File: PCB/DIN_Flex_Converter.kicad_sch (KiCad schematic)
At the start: 14 parts

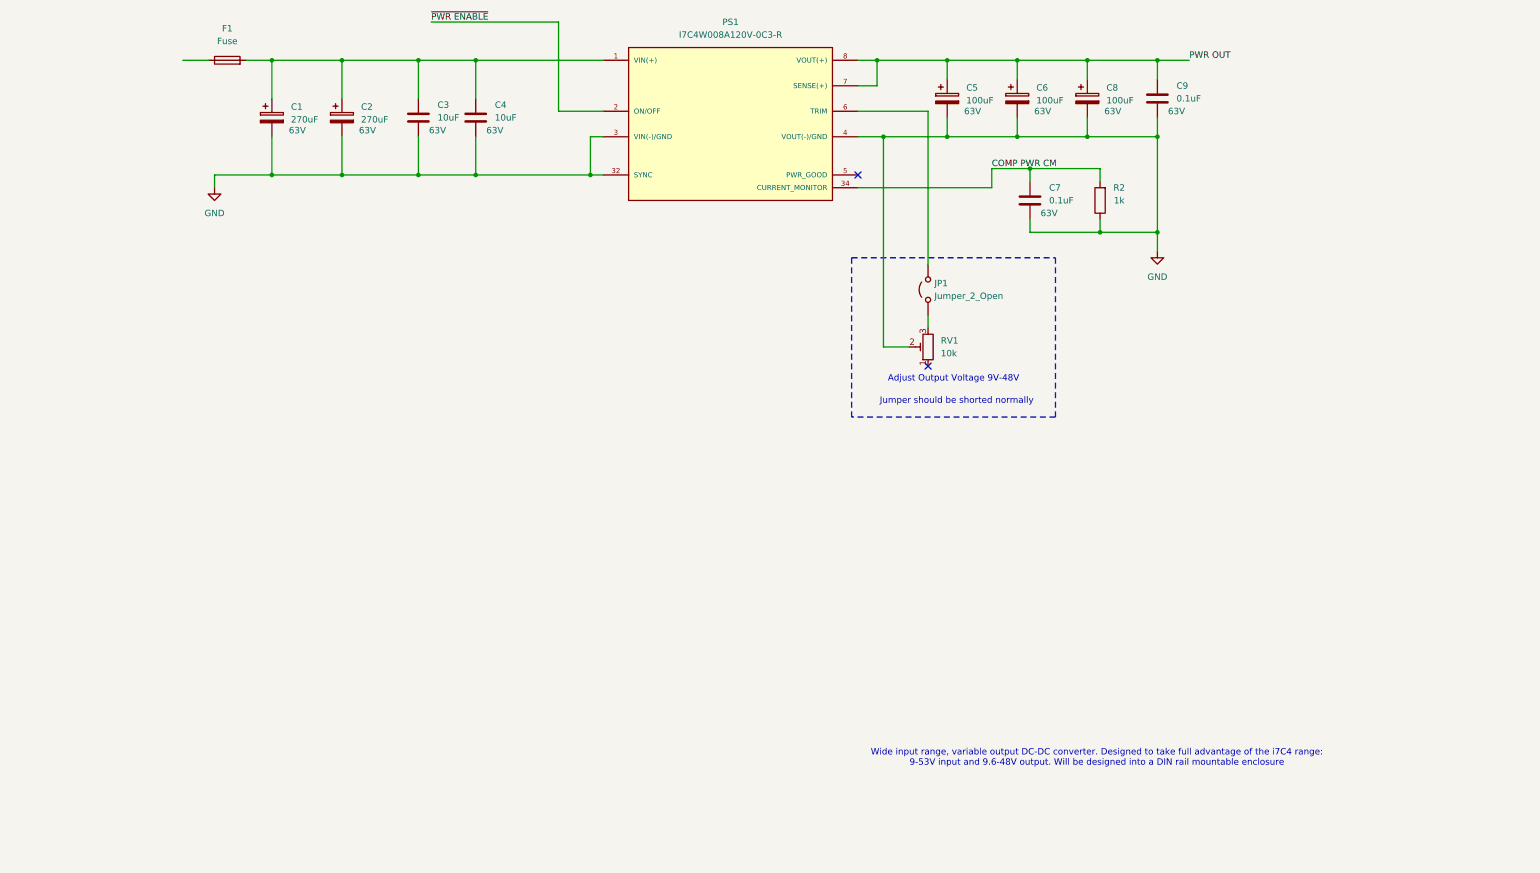
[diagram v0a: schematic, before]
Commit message: Added Trim & Linear Regulator
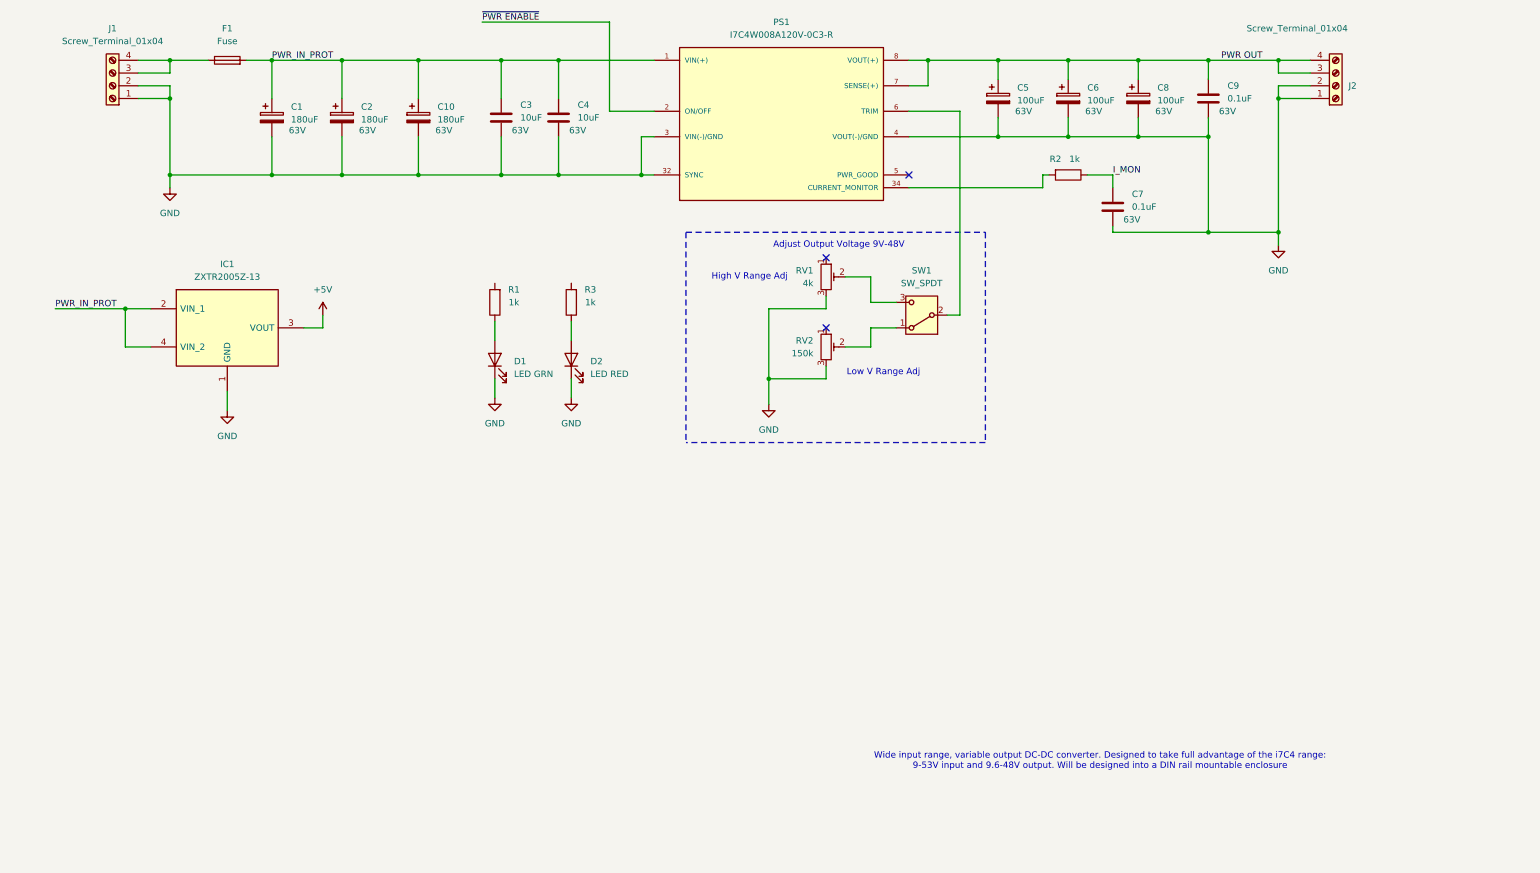
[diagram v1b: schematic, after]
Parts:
- removed JP1: Jumper_2_Open, Connector_PinHeader_2.54mm:PinHeader_1x02_P2.54mm_Vertical, symbol Jumper:Jumper_2_Open
- added C10: 180uF, Capacitor_SMD:CP_Elec_10x12.6, symbol Device:C_Polarized
- added D1: LED GRN, symbol Device:LED
- added D2: LED RED, symbol Device:LED
- added IC1: ZXTR2005Z-13, AZ7042RTRG1, symbol PSA:ZXTR2005Z-13
- added J1, J2: Screw_Terminal_01x04, symbol Connector:Screw_Terminal_01x04
- added R1, R3: 1k, Resistor_SMD:R_1206_3216Metric, symbol Device:R
- added RV2: 150k, PSA:Bourns PV37X, symbol Device:R_Potentiometer_Trim
- added SW1: SW_SPDT, symbol Switch:SW_SPDT
- C1, C2: value 270uF -> 180uF
- C9: footprint Capacitor_SMD:C_1210_3225Metric -> Capacitor_SMD:C_1206_3216Metric
- RV1: value 10k -> 4k
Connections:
- net GND: now also RV1.3, C10.2, D1.1 (K), D2.1 (K), IC1.1 (GND), J1.1 (Pin_1), J1.2 (Pin_2), J2.1 (Pin_1), J2.2 (Pin_2), RV2.3; no longer R2.1, RV1.2
- net PWR OUT: now also J2.3 (Pin_3), J2.4 (Pin_4)
- net PWR_IN_PROT: now reaches C1.1, C2.1, C3.1, C4.1, F1.2, PS1.1 (VIN(+))
- net PWR_IN_PROT: now also C10.1, IC1.2 (VIN_1), IC1.4 (VIN_2)
- net at PS1.6 (TRIM): now also SW1.2 (B)
- net at F1.1: now also J1.3 (Pin_3), J1.4 (Pin_4)
- net COMP PWR CM: no longer names the net of PS1.34 (CURRENT_MONITOR), R2.2
- net COMP PWR CM: no longer C7.1
- new net: D2.2 (A), R3.1
- new net: RV2.2, SW1.1 (A)
- new net: RV1.2, SW1.3 (C)
- new net: D1.2 (A), R1.1
- new net +5V: IC1.3 (VOUT)
- new net I_MON: C7.1, R2.1
- no-connect marks 2 -> 3
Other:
- note added: "High V Range Adj"
- note added: "Low V Range Adj"
- note removed: "Jumper should be shorted normally"
- moved on the sheet: C3, C4, C5, C6, C7, C8, PS1, R2, RV1

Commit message: Added Indication Ckt to Schematic
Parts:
- removed SW1: SW_SPDT, symbol Switch:SW_SPDT
- added J3: Conn_01x04_Socket, PSA:PHOENIX_1803293, symbol Connector:Conn_01x04_Socket
- added R4, R5: 10k, Resistor_SMD:R_1206_3216Metric, symbol Device:R
- added S1: EG1247, PSA:EG1247, symbol PSA:EG1247
- added U1: 74HC04, Package_SO:SOIC-14-16_3.9x9.9mm_P1.27mm, symbol 74xx:74HC04
- D1, D2: footprint (none) -> PSA:LED_155124RV73200
- IC1: footprint AZ7042RTRG1 -> PSA:AZ7042RTRG1
- J1, J2: footprint (none) -> PSA:PHOENIX_2200320
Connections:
- net +5V: now also R5.2, U1.14 (VCC)
- net GND: now also J3.1 (Pin_1), S1.MH1, S1.MH2, U1.7 (GND)
- net I_MON: now also J3.3 (Pin_3)
- net ~{PWR ENABLE}: now also J3.2 (Pin_2)
- net ~{PWR_GOOD}: now reaches PS1.5 (PWR_GOOD)
- net ~{PWR_GOOD}: now also J3.4 (Pin_4), R4.1, U1.1, U1.3
- net Trim: now reaches PS1.6 (TRIM)
- net Trim: now also S1.2 (COM)
- net at R3.2: now also U1.6
- net at RV2.2: now also S1.3 (NC)
- net at RV1.2: now also S1.1 (NO)
- net at R1.2: now also U1.2
- new net: U1.4, U1.5
- new net: R4.2, R5.1
- no-connect marks 3 -> 8
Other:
- moved on the sheet: D1, D2, IC1, R1, R3, RV1, RV2

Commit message: Draft Schematic & Layout
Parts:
- added H1, H2, H3, H4: MountingHole, MountingHole:MountingHole_3.2mm_M3_DIN965, symbol Mechanical:MountingHole
- added J4, J5: Conn_02x06_Top_Bottom, Connector_PinSocket_2.54mm:PinSocket_2x06_P2.54mm_Vertical_SMD, symbol Connector_Generic:Conn_02x06_Odd_Even
- J1: footprint PSA:PHOENIX_2200320 -> PSA:PHOENIX_2907774
- J2: footprint PSA:PHOENIX_2200320 -> PSA:PHOENIX_2907787
- RV1, RV2: footprint PSA:Bourns PV37X -> PSA:3009P1154LF
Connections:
- net GND: now also J4.10 (Pin_10), J4.11 (Pin_11), J4.12 (Pin_12), J4.7 (Pin_7), J4.8 (Pin_8), J4.9 (Pin_9), J5.10 (Pin_10), J5.11 (Pin_11), J5.12 (Pin_12), J5.7 (Pin_7), J5.8 (Pin_8), J5.9 (Pin_9)
- net PWR_IN: now reaches F1.1, J1.3 (Pin_3), J1.4 (Pin_4)
- net PWR_IN: now also J4.1 (Pin_1), J4.2 (Pin_2), J4.3 (Pin_3), J4.4 (Pin_4), J4.5 (Pin_5), J4.6 (Pin_6), J5.1 (Pin_1), J5.2 (Pin_2), J5.3 (Pin_3), J5.4 (Pin_4), J5.5 (Pin_5), J5.6 (Pin_6)
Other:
- moved on the sheet: D1, D2, R1, R3, R4, R5, U1A, U1B, U1C, U1G

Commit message: Layout & Route Draft Complete
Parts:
- added C11, C13: 0.1uF, Capacitor_SMD:C_1206_3216Metric, symbol Device:C
- added C12: 10uF, Capacitor_SMD:C_1210_3225Metric, symbol Device:C
- J4, J5: footprint Connector_PinSocket_2.54mm:PinSocket_2x06_P2.54mm_Vertical_SMD -> PSA:SSM-106-XXX-DV
- U1: footprint Package_SO:SOIC-14-16_3.9x9.9mm_P1.27mm -> PSA:SOIC127P600X175-14N
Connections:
- net +5V: now also C11.1, C12.1
- net GND: now also J1.3 (Pin_3), J1.4 (Pin_4), J2.3 (Pin_3), J2.4 (Pin_4), C11.2, C12.2, C13.2; no longer J1.1 (Pin_1), J1.2 (Pin_2), J2.1 (Pin_1), J2.2 (Pin_2)
- net PWR OUT: now also J2.1 (Pin_1), J2.2 (Pin_2); no longer J2.3 (Pin_3), J2.4 (Pin_4)
- net PWR_IN: now also J1.1 (Pin_1), J1.2 (Pin_2); no longer J1.3 (Pin_3), J1.4 (Pin_4)
- net PWR_IN_PROT: now also C13.1
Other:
- moved on the sheet: IC1, J1

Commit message: PCB Finalized and manufacturing files generated
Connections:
- net GND: now also U1.11, U1.13, U1.9
- no-connect marks 8 -> 5
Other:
- moved on the sheet: U1D, U1E, U1F
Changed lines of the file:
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@@
 	)
 	(junction
+		(at 106.68 152.4)
+		(diameter 0)
+		(color 0 0 0 0)
+	)
+	(junction
 		(at 140.97 54.61)
 		(diameter 0)
@@
 	)
 	(junction
+		(at 106.68 142.24)
+		(diameter 0)
+		(color 0 0 0 0)
+	)
+	(junction
 		(at 96.52 31.75)
 		(diameter 0)
@@
 	)
 	(no_connect
-		(at 238.76 132.08)
-	)
-	(no_connect
-		(at 317.5 99.06)
-	)
-	(no_connect
-		(at 317.5 119.38)
-	)
-	(no_connect
-		(at 238.76 118.11)
+		(at 124.46 130.81)
 	)
 	(no_connect
-		(at 302.26 120.65)
+		(at 238.76 132.08)
 	)
 	(no_connect
-		(at 302.26 99.06)
+		(at 124.46 142.24)
 	)
 	(no_connect
-		(at 317.5 110.49)
+		(at 124.46 152.4)
 	)
 	(no_connect
-		(at 302.26 110.49)
+		(at 238.76 118.11)
 	)
 	(wire
@@
 	(wire
 		(pts
+			(xy 106.68 142.24) (xy 109.22 142.24)
+		)
+		(stroke
+			(width 0)
+			(type default)
+		)
+	)
+	(wire
+		(pts
 			(xy 41.91 165.1) (xy 36.83 165.1)
 		)
@@
 	(wire
 		(pts
+			(xy 106.68 142.24) (xy 106.68 152.4)
+		)
+		(stroke
+			(width 0)
+			(type default)
+		)
+	)
+	(wire
+		(pts
 			(xy 50.8 85.09) (xy 46.99 85.09)
 		)
@@
 	(wire
 		(pts
+			(xy 109.22 130.81) (xy 106.68 130.81)
+		)
+		(stroke
+			(width 0)
+			(type default)
+		)
+	)
+	(wire
+		(pts
 			(xy 74.93 177.8) (xy 57.15 177.8)
 		)
@@
 	(wire
 		(pts
+			(xy 106.68 130.81) (xy 106.68 142.24)
+		)
+		(stroke
+			(width 0)
+			(type default)
+		)
+	)
+	(wire
+		(pts
 			(xy 226.06 46.99) (xy 240.03 46.99)
 		)
@@
 	(wire
 		(pts
+			(xy 106.68 152.4) (xy 109.22 152.4)
+		)
+		(stroke
+			(width 0)
+			(type default)
+		)
+	)
+	(wire
+		(pts
 			(xy 147.32 114.3) (xy 147.32 116.84)
 		)
@@
 	(wire
 		(pts
+			(xy 106.68 152.4) (xy 106.68 160.02)
+		)
+		(stroke
+			(width 0)
+			(type default)
+		)
+	)
+	(wire
+		(pts
 			(xy 40.64 34.29) (xy 46.99 34.29)
 		)
@@
 	(symbol
 		(lib_id "74xx:74HC04")
-		(at 309.88 120.65 0)
+		(at 116.84 152.4 0)
 		(unit 6)
 		(exclude_from_sim no)
@@
 		(fields_autoplaced yes)
 		(property "Reference" "U1"
-			(at 309.88 111.76 0)
+			(at 116.84 143.51 0)
 			(effects
 				(font
@@
 		)
 		(property "Value" "74HC04"
-			(at 309.88 114.3 0)
+			(at 116.84 146.05 0)
 			(effects
 				(font
@@
 		)
 		(property "Footprint" "PSA:SOIC127P600X175-14N"
-			(at 309.88 120.65 0)
+			(at 116.84 152.4 0)
 			(effects
 				(font
@@
 		)
 		(property "Datasheet" "https://assets.nexperia.com/documents/data-sheet/74HC_HCT04.pdf"
-			(at 309.88 120.65 0)
+			(at 116.84 152.4 0)
 			(effects
 				(font
@@
 		)
 		(property "Description" "Hex Inverter"
-			(at 309.88 120.65 0)
+			(at 116.84 152.4 0)
 			(effects
 				(font
@@
 		(lib_name "GND_14")
 		(lib_id "power:GND")
+		(at 106.68 160.02 0)
+		(unit 1)
+		(exclude_from_sim no)
+		(in_bom yes)
+		(on_board yes)
+		(dnp no)
+		(fields_autoplaced yes)
+		(property "Reference" "#PWR015"
+			(at 106.68 166.37 0)
+			(effects
+				(font
+					(size 1.27 1.27)
+				)
+				(hide yes)
+			)
+		)
+		(property "Value" "GND"
+			(at 106.68 165.1 0)
+			(effects
+				(font
+					(size 1.27 1.27)
+				)
+			)
+		)
+		(property "Footprint" ""
+			(at 106.68 160.02 0)
+			(effects
+				(font
+					(size 1.27 1.27)
+				)
+				(hide yes)
+			)
+		)
+		(property "Datasheet" ""
+			(at 106.68 160.02 0)
+			(effects
+				(font
+					(size 1.27 1.27)
+				)
+				(hide yes)
+			)
+		)
+		(property "Description" ""
+			(at 106.68 160.02 0)
+			(effects
+				(font
+					(size 1.27 1.27)
+				)
+				(hide yes)
+			)
+		)
+		(pin "1"
+		)
+		(instances
+			(project "DIN_Flex_Converter"
+				(path "/e44269d9-3860-4750-a5c6-e30e8b477b13"
+					(reference "#PWR015")
+					(unit 1)
+				)
+			)
+		)
+	)
+	(symbol
+		(lib_name "GND_14")
+		(lib_id "power:GND")
 		(at 257.81 134.62 270)
 		(unit 1)
@@
 	(symbol
 		(lib_id "74xx:74HC04")
-		(at 309.88 110.49 0)
+		(at 116.84 142.24 0)
 		(unit 5)
 		(exclude_from_sim no)
@@
 		(fields_autoplaced yes)
 		(property "Reference" "U1"
-			(at 309.88 101.6 0)
+			(at 116.84 133.35 0)
 			(effects
 				(font
@@
 		)
 		(property "Value" "74HC04"
-			(at 309.88 104.14 0)
+			(at 116.84 135.89 0)
 			(effects
 				(font
@@
 		)
 		(property "Footprint" "PSA:SOIC127P600X175-14N"
-			(at 309.88 110.49 0)
+			(at 116.84 142.24 0)
 			(effects
 				(font
@@
 		)
 		(property "Datasheet" "https://assets.nexperia.com/documents/data-sheet/74HC_HCT04.pdf"
-			(at 309.88 110.49 0)
+			(at 116.84 142.24 0)
 			(effects
 				(font
@@
 		)
 		(property "Description" "Hex Inverter"
-			(at 309.88 110.49 0)
+			(at 116.84 142.24 0)
 			(effects
 				(font
@@
 	(symbol
 		(lib_id "74xx:74HC04")
-		(at 309.88 99.06 0)
+		(at 116.84 130.81 0)
 		(unit 4)
 		(exclude_from_sim no)
@@
 		(fields_autoplaced yes)
 		(property "Reference" "U1"
-			(at 309.88 90.17 0)
+			(at 116.84 121.92 0)
 			(effects
 				(font
@@
 		)
 		(property "Value" "74HC04"
-			(at 309.88 92.71 0)
+			(at 116.84 124.46 0)
 			(effects
 				(font
@@
 		)
 		(property "Footprint" "PSA:SOIC127P600X175-14N"
-			(at 309.88 99.06 0)
+			(at 116.84 130.81 0)
 			(effects
 				(font
@@
 		)
 		(property "Datasheet" "https://assets.nexperia.com/documents/data-sheet/74HC_HCT04.pdf"
-			(at 309.88 99.06 0)
+			(at 116.84 130.81 0)
 			(effects
 				(font
@@
 		)
 		(property "Description" "Hex Inverter"
-			(at 309.88 99.06 0)
+			(at 116.84 130.81 0)
 			(effects
 				(font
